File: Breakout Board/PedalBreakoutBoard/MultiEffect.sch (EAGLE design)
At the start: 52 parts, among them IC1 LD1117V, IC2 MCP6004P, U1 OPA1652AID

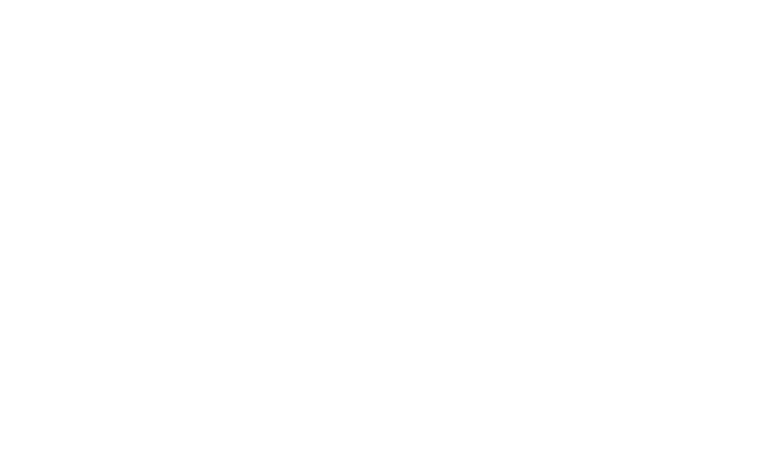
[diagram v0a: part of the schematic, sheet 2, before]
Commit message: DP-6 - Add connections for OLED
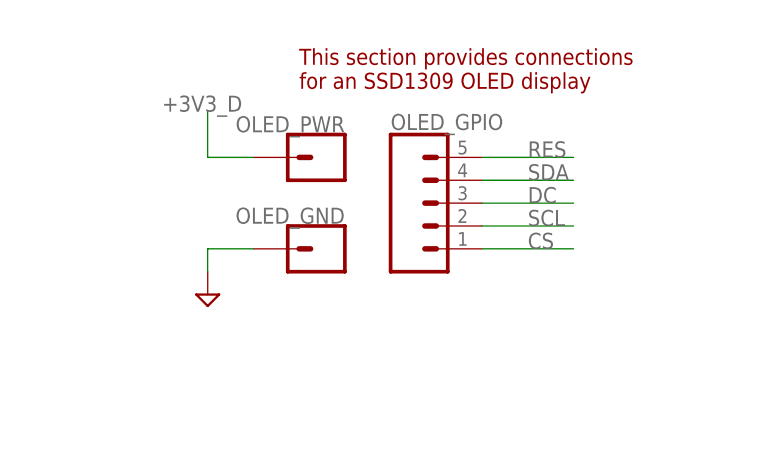
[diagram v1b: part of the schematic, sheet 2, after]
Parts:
- added OLED_GND, OLED_PWR: (no value), SparkFun-Connectors:CONN_01
- added OLED_GPIO: (no value), SparkFun-Connectors:CONN_05
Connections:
- new net +3V3_D: OLED_PWR.1, SEED.+3V3_D
- new net CS: OLED_GPIO.1, SEED.GPIO8(SPI1_NSS)
- new net DC: OLED_GPIO.3, SEED.GPIO10(SPI1_MISO)
- new net RES: OLED_GPIO.5, SEED.GPIO12(I2C1_SCL)
- new net SCL: OLED_GPIO.2, SEED.GPIO9(SPI1_SCK)
- new net SDA: OLED_GPIO.4, SEED.GPIO11(SPI1_MOSI)
- net GND: now also OLED_GND.1
- net SPDT1_1: now also SEED.GPIO13(I2C1_SDA); no longer SEED.GPIO11(SPI1_MOSI)
- net SPDT1_2: now also SEED.GPIO14(USART1_TX); no longer SEED.GPIO12(I2C1_SCL)
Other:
- note added: "This section provides connections for an SSD1309 OLED display"
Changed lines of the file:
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@@
 <schematic_group name="AUDIO_PWR"/>
 <schematic_group name="AUDIO_JACKS"/>
+<schematic_group name="OLED"/>
 </groups>
 <parts>
@@
 <part name="SUPPLY12" library="supply2" library_urn="urn:adsk.eagle:library:372" deviceset="GND" device=""/>
 <part name="ENC_GPIO" library="SparkFun-Connectors" library_urn="urn:adsk.eagle:library:513" deviceset="CONN_03" device="" package3d_urn="urn:adsk.eagle:package:38063/1"/>
+<part name="OLED_GPIO" library="SparkFun-Connectors" library_urn="urn:adsk.eagle:library:513" deviceset="CONN_05" device="" package3d_urn="urn:adsk.eagle:package:38104/1"/>
+<part name="OLED_PWR" library="SparkFun-Connectors" library_urn="urn:adsk.eagle:library:513" deviceset="CONN_01" device="" package3d_urn="urn:adsk.eagle:package:38028/1"/>
+<part name="OLED_GND" library="SparkFun-Connectors" library_urn="urn:adsk.eagle:library:513" deviceset="CONN_01" device="" package3d_urn="urn:adsk.eagle:package:38028/1"/>
+<part name="SUPPLY22" library="supply2" library_urn="urn:adsk.eagle:library:372" deviceset="GND" device=""/>
 </parts>
 <sheets>
@@
 <net name="SPDT1_1" class="0">
 <segment>
-<pinref part="SEED" gate="G$1" pin="GPIO11(SPI1_MOSI)"/>
-<wire x1="73.66" y1="88.9" x2="58.42" y2="88.9" width="0.1524" layer="91"/>
-<label x="58.42" y="88.9" size="1.778" layer="95"/>
+<pinref part="SEED" gate="G$1" pin="GPIO13(I2C1_SDA)"/>
+<wire x1="73.66" y1="83.82" x2="58.42" y2="83.82" width="0.1524" layer="91"/>
+<label x="58.42" y="83.82" size="1.778" layer="95"/>
 </segment>
 </net>
 <net name="SPDT1_2" class="0">
 <segment>
-<pinref part="SEED" gate="G$1" pin="GPIO12(I2C1_SCL)"/>
-<wire x1="73.66" y1="86.36" x2="58.42" y2="86.36" width="0.1524" layer="91"/>
-<label x="58.42" y="86.36" size="1.778" layer="95"/>
+<pinref part="SEED" gate="G$1" pin="GPIO14(USART1_TX)"/>
+<wire x1="73.66" y1="81.28" x2="58.42" y2="81.28" width="0.1524" layer="91"/>
+<label x="58.42" y="81.28" size="1.778" layer="95"/>
 </segment>
 </net>
@@
 </segment>
 </net>
+<net name="+3V3_D" class="0">
+<segment>
+<pinref part="SEED" gate="G$1" pin="+3V3_D"/>
+<wire x1="134.62" y1="109.22" x2="149.86" y2="109.22" width="0.1524" layer="91"/>
+<label x="139.7" y="109.22" size="1.778" layer="95"/>
+</segment>
+</net>
+<net name="SCL" class="0">
+<segment>
+<pinref part="SEED" gate="G$1" pin="GPIO9(SPI1_SCK)"/>
+<wire x1="73.66" y1="93.98" x2="58.42" y2="93.98" width="0.1524" layer="91"/>
+<label x="58.42" y="93.98" size="1.778" layer="95"/>
+</segment>
+</net>
+<net name="SDA" class="0">
+<segment>
+<pinref part="SEED" gate="G$1" pin="GPIO11(SPI1_MOSI)"/>
+<wire x1="73.66" y1="88.9" x2="58.42" y2="88.9" width="0.1524" layer="91"/>
+<label x="58.42" y="88.9" size="1.778" layer="95"/>
+</segment>
+</net>
+<net name="DC" class="0">
+<segment>
+<pinref part="SEED" gate="G$1" pin="GPIO10(SPI1_MISO)"/>
+<wire x1="73.66" y1="91.44" x2="58.42" y2="91.44" width="0.1524" layer="91"/>
+<label x="58.42" y="91.44" size="1.778" layer="95"/>
+</segment>
+</net>
+<net name="CS" class="0">
+<segment>
+<pinref part="SEED" gate="G$1" pin="GPIO8(SPI1_NSS)"/>
+<wire x1="73.66" y1="96.52" x2="58.42" y2="96.52" width="0.1524" layer="91"/>
+<label x="58.42" y="96.52" size="1.778" layer="95"/>
+</segment>
+</net>
+<net name="RES" class="0">
+<segment>
+<pinref part="SEED" gate="G$1" pin="GPIO12(I2C1_SCL)"/>
+<wire x1="73.66" y1="86.36" x2="58.42" y2="86.36" width="0.1524" layer="91"/>
+<label x="58.42" y="86.36" size="1.778" layer="95"/>
+</segment>
+</net>
 </nets>
 </sheet>
@@
 <text x="93.98" y="5.08" size="1.778" layer="94" grouprefs="LED">This section provides connections for 4 LEDs,
 each behind a 330Ohm resistor</text>
+<text x="139.7" y="58.42" size="1.778" layer="94" grouprefs="OLED">This section provides connections
+for an SSD1309 OLED display</text>
 </plain>
 <instances>
@@
 <attribute name="NAME" x="129.54" y="0.508" size="1.778" layer="95" font="vector"/>
 </instance>
-<instance part="ENC_GND" gate="G$1" x="-45.72" y="-12.7" smashed="yes" rot="R180">
+<instance part="ENC_GND" gate="G$1" x="-45.72" y="-12.7" smashed="yes" rot="R180" grouprefs="ENCODER">
 <attribute name="VALUE" x="-43.18" y="-7.874" size="1.778" layer="96" font="vector" rot="R180"/>
 <attribute name="NAME" x="-43.18" y="-8.128" size="1.778" layer="95" font="vector" rot="R180"/>
 </instance>
-<instance part="SUPPLY12" gate="GND" x="-58.42" y="-17.78" smashed="yes"/>
-<instance part="ENC_GPIO" gate="J$1" x="-38.1" y="-5.08" smashed="yes">
+<instance part="SUPPLY12" gate="GND" x="-58.42" y="-17.78" smashed="yes" grouprefs="ENCODER"/>
+<instance part="ENC_GPIO" gate="J$1" x="-38.1" y="-5.08" smashed="yes" grouprefs="ENCODER">
 <attribute name="VALUE" x="-40.64" y="-12.446" size="1.778" layer="96" font="vector"/>
 <attribute name="NAME" x="-40.64" y="0.508" size="1.778" layer="95" font="vector"/>
 </instance>
+<instance part="OLED_GPIO" gate="G$1" x="152.4" y="45.72" smashed="yes" grouprefs="OLED">
+<attribute name="VALUE" x="149.86" y="35.814" size="1.778" layer="96" font="vector"/>
+<attribute name="NAME" x="149.86" y="53.848" size="1.778" layer="95" font="vector"/>
+</instance>
+<instance part="OLED_PWR" gate="G$1" x="142.24" y="50.8" smashed="yes" rot="R180" grouprefs="OLED">
+<attribute name="VALUE" x="144.78" y="55.626" size="1.778" layer="96" font="vector" rot="R180"/>
+<attribute name="NAME" x="144.78" y="55.372" size="1.778" layer="95" font="vector" rot="R180"/>
+</instance>
+<instance part="OLED_GND" gate="G$1" x="142.24" y="40.64" smashed="yes" rot="R180" grouprefs="OLED">
+<attribute name="VALUE" x="144.78" y="45.466" size="1.778" layer="96" font="vector" rot="R180"/>
+<attribute name="NAME" x="144.78" y="45.212" size="1.778" layer="95" font="vector" rot="R180"/>
+</instance>
+<instance part="SUPPLY22" gate="GND" x="129.54" y="35.56" smashed="yes" grouprefs="OLED"/>
 </instances>
 <busses>
@@
 <wire x1="-58.42" y1="-12.7" x2="-58.42" y2="-15.24" width="0.1524" layer="91"/>
 </segment>
+<segment>
+<pinref part="OLED_GND" gate="G$1" pin="1"/>
+<pinref part="SUPPLY22" gate="GND" pin="GND"/>
+<wire x1="134.62" y1="40.64" x2="129.54" y2="40.64" width="0.1524" layer="91" grouprefs="OLED"/>
+<wire x1="129.54" y1="40.64" x2="129.54" y2="38.1" width="0.1524" layer="91" grouprefs="OLED"/>
+</segment>
 </net>
 <net name="POT4" class="0">
@@
 </segment>
 </net>
+<net name="+3V3_D" class="0">
+<segment>
+<pinref part="OLED_PWR" gate="G$1" pin="1"/>
+<wire x1="134.62" y1="50.8" x2="129.54" y2="50.8" width="0.1524" layer="91" grouprefs="OLED"/>
+<wire x1="129.54" y1="50.8" x2="129.54" y2="55.88" width="0.1524" layer="91" grouprefs="OLED"/>
+<label x="124.46" y="55.88" size="1.778" layer="95" grouprefs="OLED"/>
+</segment>
+</net>
+<net name="CS" class="0">
+<segment>
+<pinref part="OLED_GPIO" gate="G$1" pin="1"/>
+<wire x1="160.02" y1="40.64" x2="170.18" y2="40.64" width="0.1524" layer="91" grouprefs="OLED"/>
+<label x="165.1" y="40.64" size="1.778" layer="95" grouprefs="OLED"/>
+</segment>
+</net>
+<net name="SCL" class="0">
+<segment>
+<pinref part="OLED_GPIO" gate="G$1" pin="2"/>
+<wire x1="160.02" y1="43.18" x2="170.18" y2="43.18" width="0.1524" layer="91"/>
+<label x="165.1" y="43.18" size="1.778" layer="95"/>
+</segment>
+</net>
+<net name="DC" class="0">
+<segment>
+<pinref part="OLED_GPIO" gate="G$1" pin="3"/>
+<wire x1="160.02" y1="45.72" x2="170.18" y2="45.72" width="0.1524" layer="91"/>
+<label x="165.1" y="45.72" size="1.778" layer="95"/>
+</segment>
+</net>
+<net name="SDA" class="0">
+<segment>
+<pinref part="OLED_GPIO" gate="G$1" pin="4"/>
+<wire x1="160.02" y1="48.26" x2="170.18" y2="48.26" width="0.1524" layer="91"/>
+<label x="165.1" y="48.26" size="1.778" layer="95"/>
+</segment>
+</net>
+<net name="RES" class="0">
+<segment>
+<pinref part="OLED_GPIO" gate="G$1" pin="5"/>
+<wire x1="160.02" y1="50.8" x2="170.18" y2="50.8" width="0.1524" layer="91"/>
+<label x="165.1" y="50.8" size="1.778" layer="95"/>
+</segment>
+</net>

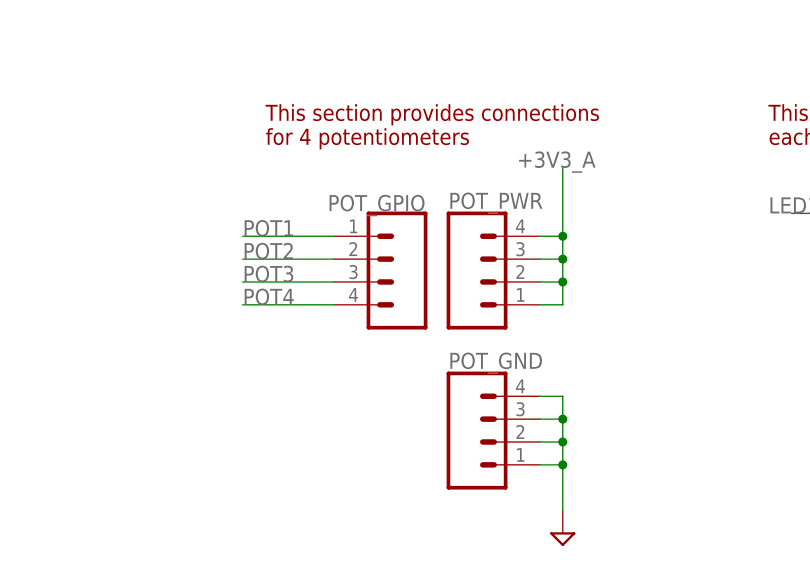
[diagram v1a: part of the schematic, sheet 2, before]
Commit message: DP-6 - Add additional POT for output volume
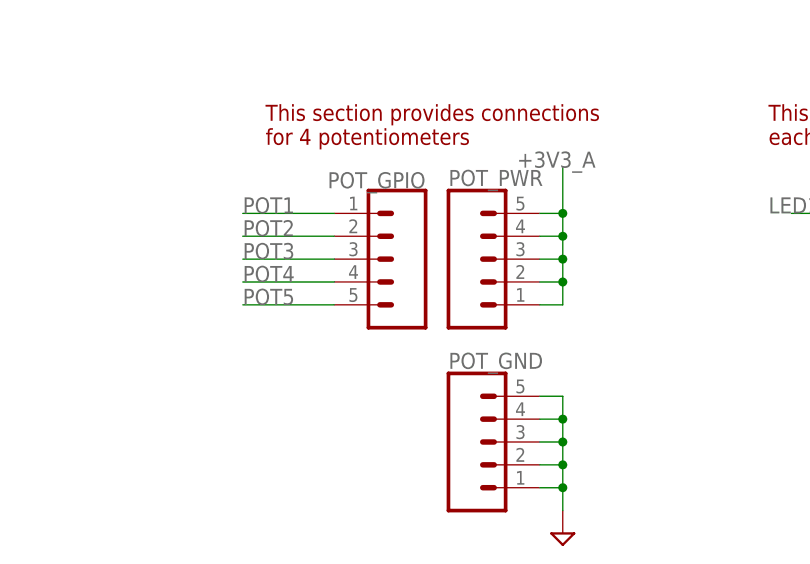
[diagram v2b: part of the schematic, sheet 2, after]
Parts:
- POT_GND, POT_GPIO, POT_PWR: device SparkFun-Connectors:CONN_04 -> SparkFun-Connectors:CONN_05
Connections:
- new net POT5: POT_GPIO.5, SEED.GPIO22(ADC1_INP4)
- net +3V3_A: now also POT_PWR.5
- net GND: now also POT_GND.5
- net POT1: now also SEED.GPIO26(SAI2_SD_B); no longer SEED.GPIO24(DAC1_OUT1)
- net POT2: now also SEED.GPIO25(SAI2_MCLK_B); no longer SEED.GPIO23(DAC1_OUT2)
- net POT3: now also SEED.GPIO24(DAC1_OUT1); no longer SEED.GPIO22(ADC1_INP4)
- net POT4: now also SEED.GPIO23(DAC1_OUT2); no longer SEED.GPIO21(ADC1_INP11)

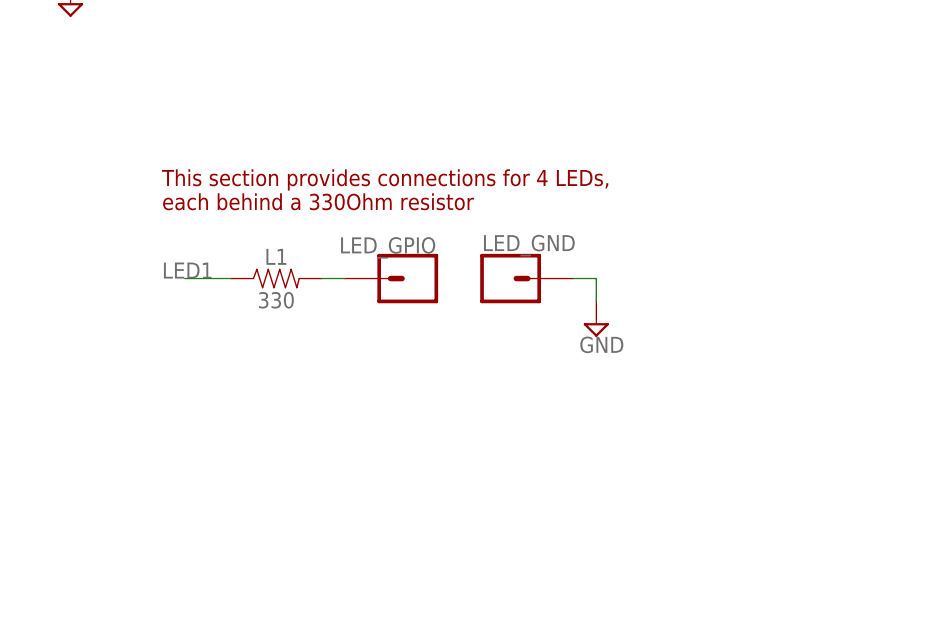
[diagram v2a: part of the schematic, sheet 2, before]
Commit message: DP-6 - Add additional LEDs
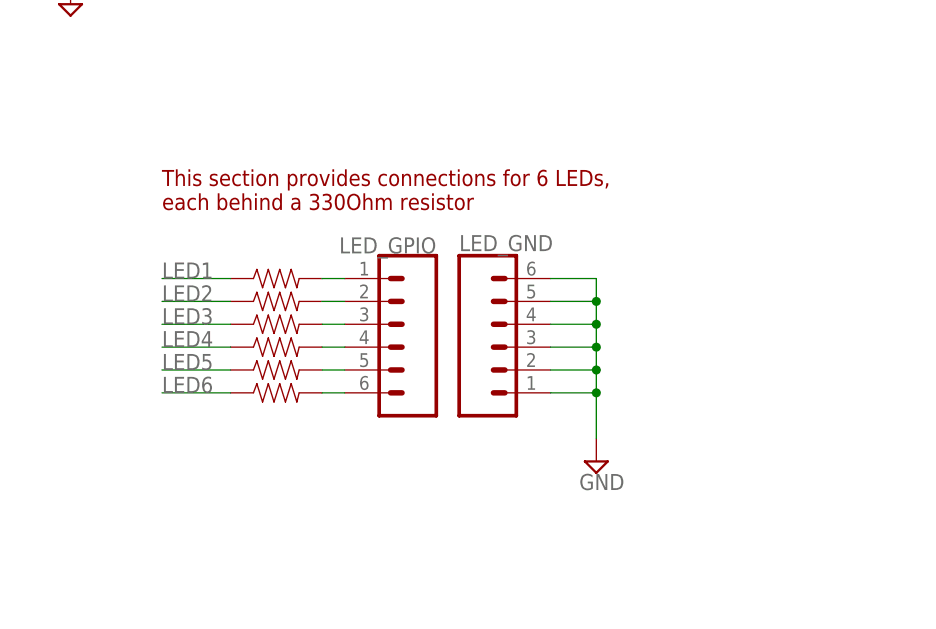
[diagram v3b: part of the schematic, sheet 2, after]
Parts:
- added L2, L3, L4, L6, L7: 330, SparkFun-Resistors:330OHM-HORIZ-1/10W-5%
- LED_GND, LED_GPIO: device SparkFun-Connectors:CONN_01 -> SparkFun-Connectors:CONN_06SILK_FEMALE_PTH
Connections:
- new net LED2: L2.1, SEED.GPIO20(ADC1_INP3)
- new net LED3: L3.1, SEED.GPIO19(ADC1_INP7)
- new net LED4: L4.1, SEED.GPIO18(ADC1_INP5)
- new net LED5: L6.1, SEED.GPIO17(ADC1_INP15)
- new net LED6: L7.1, SEED.GPIO16(ADC1_INP10)
- new net N$11: L6.2, LED_GPIO.5
- new net N$16: L7.2, LED_GPIO.6
- new net N$3: L2.2, LED_GPIO.2
- new net N$4: L3.2, LED_GPIO.3
- new net N$5: L4.2, LED_GPIO.4
- new net SPST2: SEED.GPIO2(SDMMC1_D3)
- new net SPST3: SEED.GPIO3(SDMMC1_D2)
- new net SPST4: SEED.GPIO4(SDMMC1_D1)
- new net SPST5: SEED.GPIO5(SDMMC1_D0)
- new net SPST6: SEED.GPIO6(SDMMC1_CMD)
- net GND: now also LED_GND.2, LED_GND.3, LED_GND.4, LED_GND.5, LED_GND.6
- net LED1: now also SEED.GPIO21(ADC1_INP11); no longer SEED.GPIO19(ADC1_INP7)
- net SPST1: now also SEED.GPIO1(USB_HS_ID); no longer SEED.GPIO6(SDMMC1_CMD)
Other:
- note added: "This section provides connections for 6 LEDs, each behind a 330Ohm resistor"
- note removed: "This section provides connections for 4 LEDs, each behind a 330Ohm resistor"

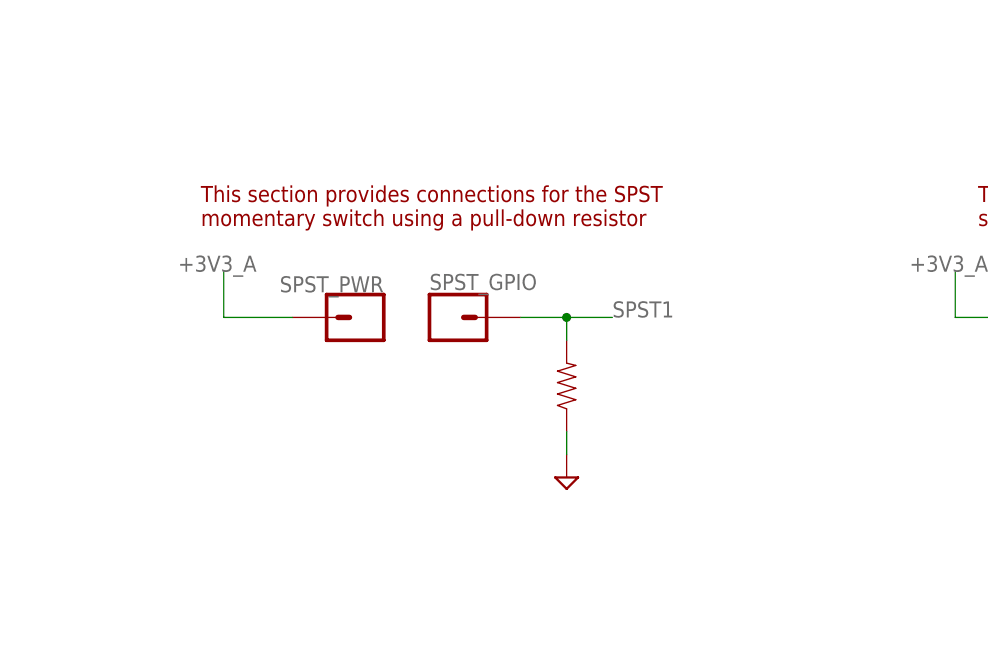
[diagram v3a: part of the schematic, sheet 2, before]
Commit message: DP-6 - Add additional SPST connections
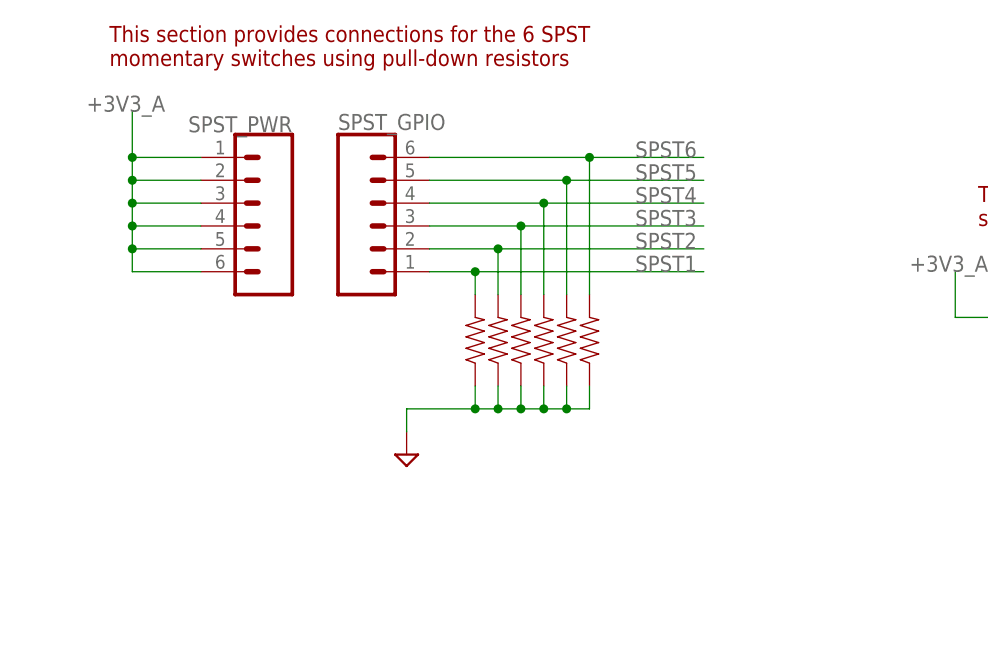
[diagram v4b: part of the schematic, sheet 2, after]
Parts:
- added S2, S3, S4, S5, S6: 10k, SparkFun-Resistors:10KOHM-HORIZ-1/4W-5%
- SPST_GPIO, SPST_PWR: device SparkFun-Connectors:CONN_01 -> SparkFun-Connectors:CONN_06SILK_FEMALE_PTH
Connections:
- net +3V3_A: now also SPST_PWR.2, SPST_PWR.3, SPST_PWR.4, SPST_PWR.5, SPST_PWR.6
- net GND: now also S2.1, S3.1, S4.1, S5.1, S6.1
- net SPST2: now also S2.2, SPST_GPIO.2
- net SPST3: now also S3.2, SPST_GPIO.3
- net SPST4: now also S4.2, SPST_GPIO.4
- net SPST5: now also S5.2, SPST_GPIO.5
- net SPST6: now also S6.2, SPST_GPIO.6
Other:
- note added: "This section provides connections for the 6 SPST momentary switches using pull-down resistors"
- note removed: "This section provides connections for the SPST momentary switch using a pull-down resistor"
